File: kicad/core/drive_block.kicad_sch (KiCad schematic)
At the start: 10 parts, among them J20 N_HSn, J21 N_LSn, Q10 FDS8958A, U20 TC4427A

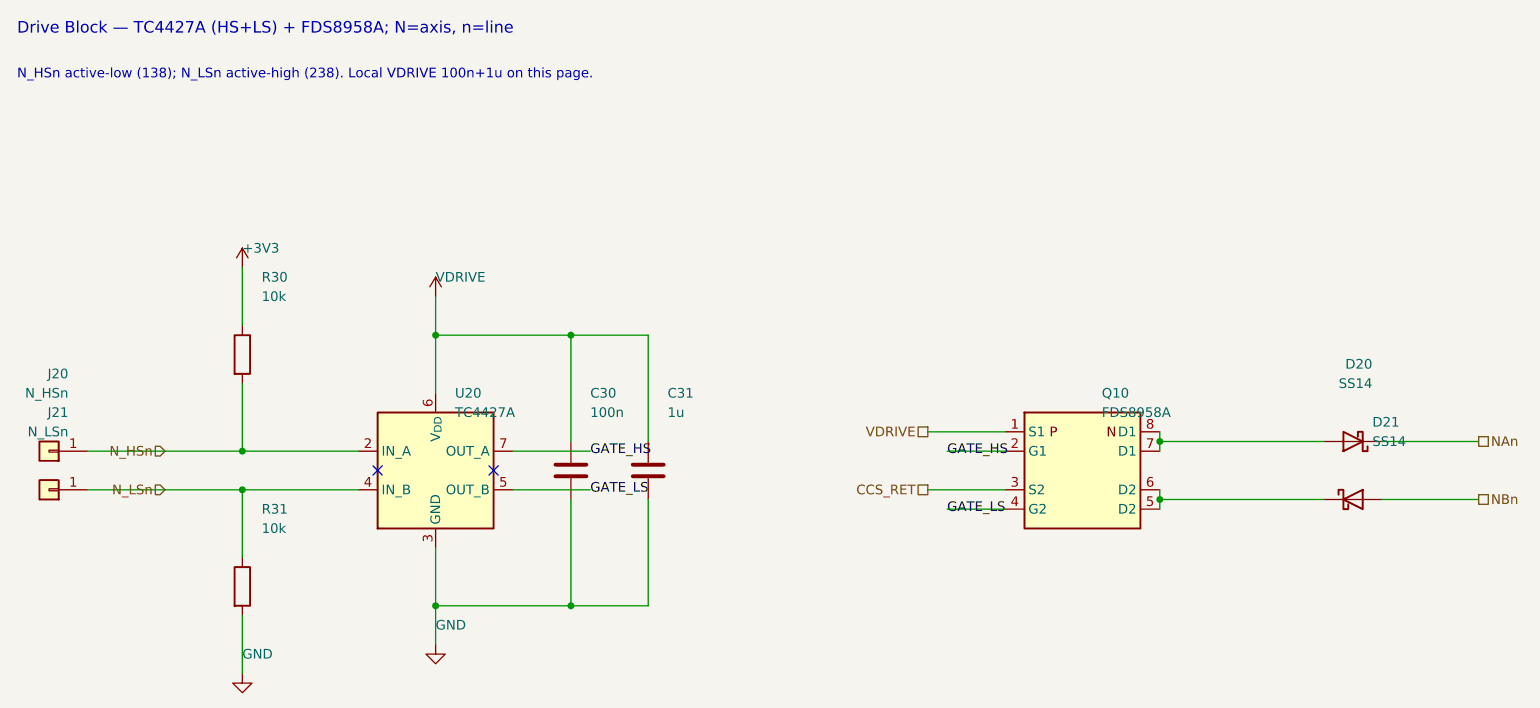
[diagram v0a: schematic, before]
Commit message: Prove the 2×2 access cycle from the address pins through decode, drive, and the sense latch.
Three current sinks, the diode matrix, and drive groups 0--7 are on the schematic. The four-core decks are the gate; weave inductance is still an open input.
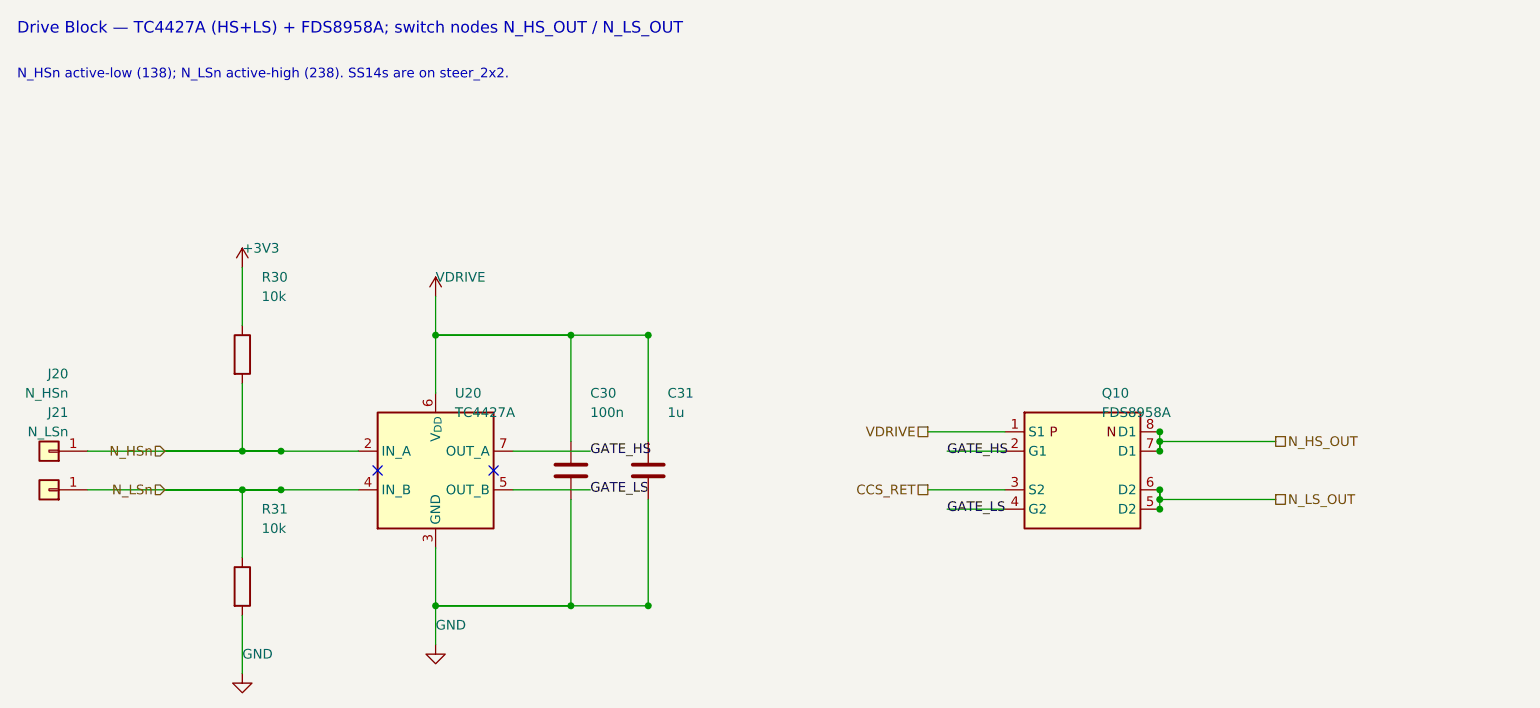
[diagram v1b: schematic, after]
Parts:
- removed D20, D21: SS14, Diode_SMD:D_SMA, symbol Diode:SS14
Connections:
- net N_LS_OUT: now reaches Q10.5 (D2), Q10.6 (D2)
- net N_HS_OUT: now reaches Q10.7 (D1), Q10.8 (D1)
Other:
- note added: "Drive Block — TC4427A (HS+LS) + FDS8958A; switch nodes N_HS_OUT / N_LS_OUT"
- note added: "N_HSn active-low (138); N_LSn active-high (238). SS14s are on steer_2x2."
- note removed: "Drive Block — TC4427A (HS+LS) + FDS8958A; N=axis, n=line"
- note removed: "N_HSn active-low (138); N_LSn active-high (238). Local VDRIVE 100n+1u on this page."

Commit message: Scaled to 64x64 and paying heavy due. We can learn if we have to... I guess.
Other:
- note added: "N_HSn active-low (138); N_LSn active-high (238). SS14s are on steer_64."
- note removed: "N_HSn active-low (138); N_LSn active-high (238). SS14s are on steer_2x2."
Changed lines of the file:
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@@
 		(effects (font (size 1.524 1.524)) (justify left))
 	)
-	(text "N_HSn active-low (138); N_LSn active-high (238). SS14s are on steer_2x2."
+	(text "N_HSn active-low (138); N_LSn active-high (238). SS14s are on steer_64."
 		(exclude_from_sim no)
 		(at 20 18 0)
